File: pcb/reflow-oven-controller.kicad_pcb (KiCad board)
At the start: 2 copper layers, 55 x 100 mm, 67 parts, among them J1 12V_IN, J10 RELAY_4, J11 RELAY_OPT, J12 HEADER, J14 DISPLAY, J2 USB, J3 TEMP_1, J4 TEMP_2, J7 RELAY_1, J8 RELAY_2, J9 RELAY_3, U1 TPS5430DDA, U2 AMS1117-3.3, U3 RP2040, U4 MAX31855KASA, U5 MAX31855KASA, U6 W25Q128JVS, U7 ULN2003A, Y1 X322512MSB4SI

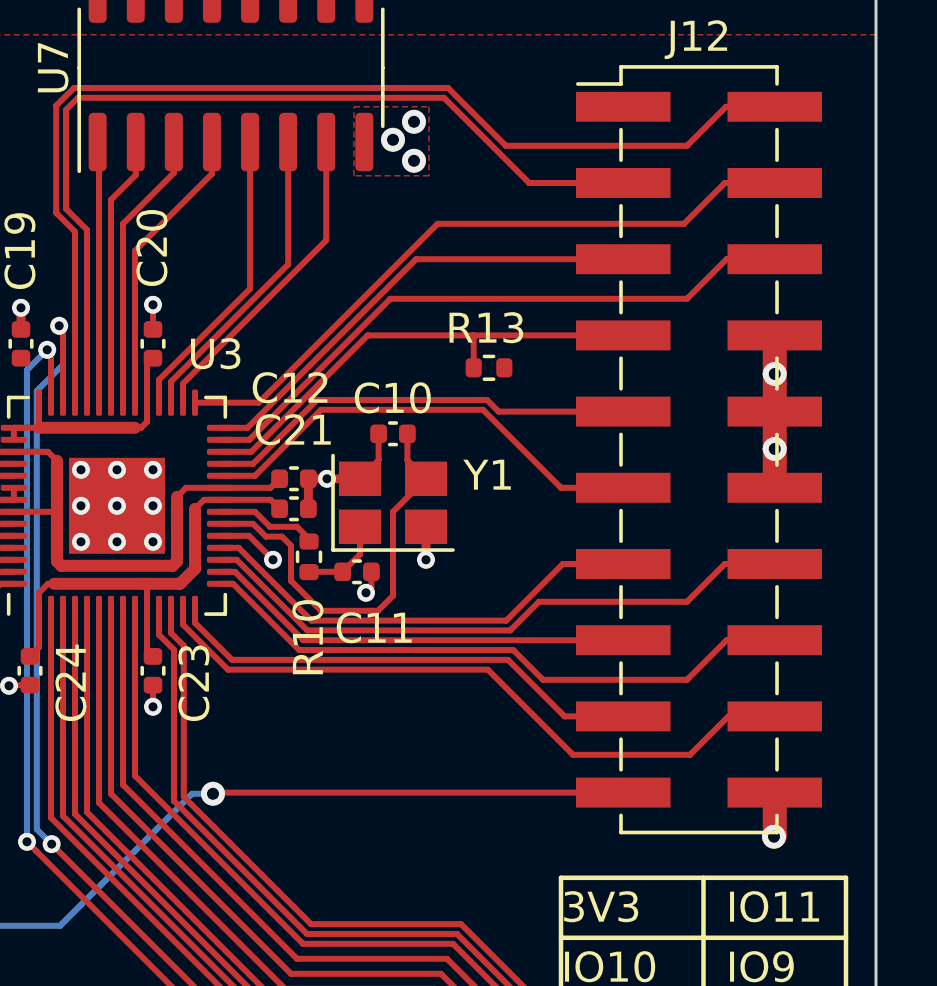
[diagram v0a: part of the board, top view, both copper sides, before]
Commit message: Add missing 3D models
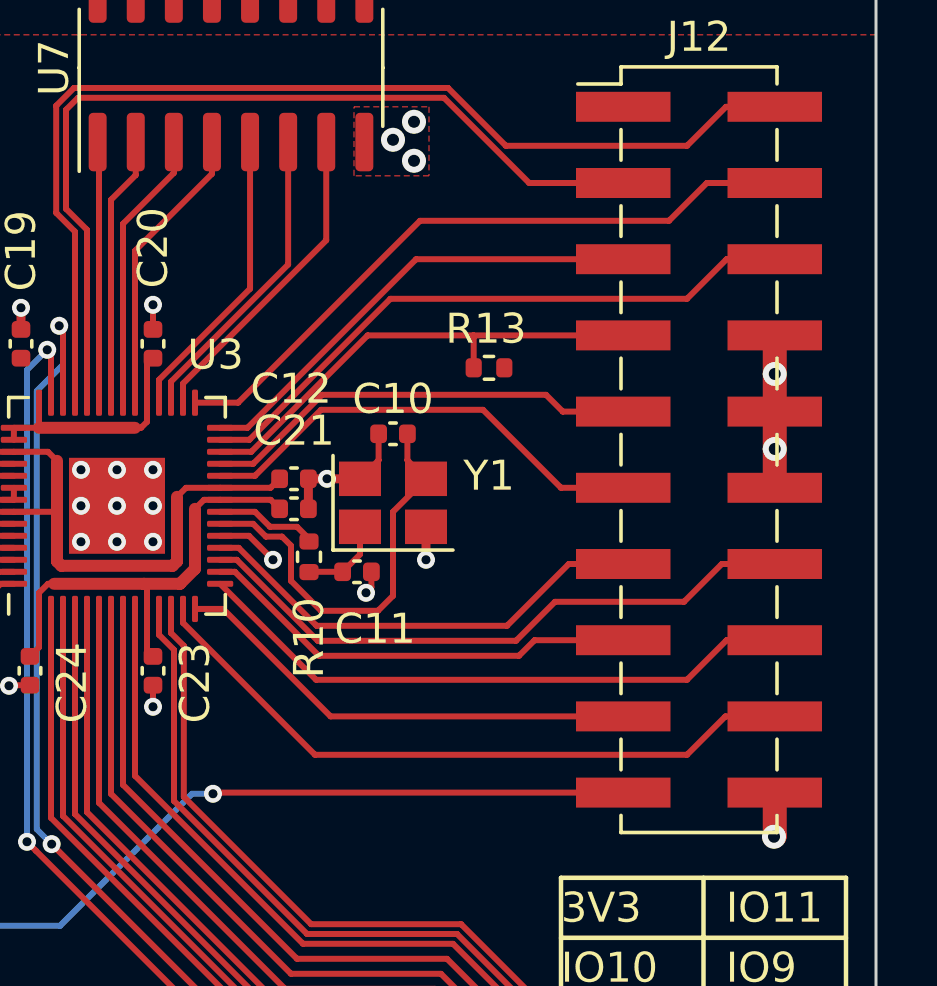
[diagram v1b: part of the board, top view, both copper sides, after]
